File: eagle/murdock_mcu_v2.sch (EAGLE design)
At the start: 30 parts, among them IC1 MPU-9150, IC2 LT1763CS8-3.3, IC3 STM32F4XX_64, U1 USD-SOCKETNEW, X1 USBSMD, X2 MURDOCK_STACK

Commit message: updated labels
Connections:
- removed net A10: IC3G$2.PORTA_10, X2.SP1
- new net C11: IC3G$4.PORTC_11, X2.SP1
- net MISO: now also IC3G$3.PORTB_4; no longer IC3G$4.PORTC_11
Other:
- note added: "1_RX"
- note added: "UART4 = GPS"
- note added: "USART1 = SBUS"
- note added: "USART3 = SP1"
- note added: "USART6 = SP2"
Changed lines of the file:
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@@
 <plain>
 <text x="-93.98" y="60.96" size="1.778" layer="91">defined value on the bootloader pins</text>
+<text x="96.52" y="149.86" size="2.54" layer="94">UART4 = GPS</text>
+<text x="96.52" y="165.1" size="2.54" layer="94">USART1 = SBUS</text>
+<text x="96.52" y="139.7" size="2.54" layer="94">USART6 = SP2</text>
+<text x="96.52" y="157.48" size="2.54" layer="94">USART3 = SP1</text>
+<text x="17.78" y="127" size="1.778" layer="91">1_RX</text>
 </plain>
 <instances>
@@
 </segment>
 </net>
-<net name="A10" class="0">
-<segment>
-<pinref part="X2" gate="G$1" pin="SP1"/>
-<wire x1="96.52" y1="22.86" x2="86.36" y2="22.86" width="0.1524" layer="91"/>
-<label x="86.36" y="22.86" size="1.778" layer="95"/>
-</segment>
-<segment>
-<pinref part="IC3" gate="G$2" pin="PORTA_10"/>
-<wire x1="-17.78" y1="142.24" x2="-25.4" y2="142.24" width="0.1524" layer="91"/>
-<label x="-25.4" y="142.24" size="1.778" layer="95"/>
-</segment>
-</net>
 <net name="C7" class="0">
 <segment>
@@
 <net name="MISO" class="0">
 <segment>
-<pinref part="IC3" gate="G$4" pin="PORTC_11"/>
-<wire x1="-7.62" y1="48.26" x2="-17.78" y2="48.26" width="0.1524" layer="91"/>
-<label x="-17.78" y="48.26" size="1.778" layer="95"/>
-</segment>
-<segment>
 <pinref part="U1" gate="G$1" pin="DO"/>
 <wire x1="50.8" y1="27.94" x2="38.1" y2="27.94" width="0.1524" layer="91"/>
 <label x="38.1" y="27.94" size="1.778" layer="95"/>
+</segment>
+<segment>
+<pinref part="IC3" gate="G$3" pin="PORTB_4"/>
+<wire x1="38.1" y1="111.76" x2="30.48" y2="111.76" width="0.1524" layer="91"/>
+<label x="30.48" y="111.76" size="1.778" layer="95"/>
 </segment>
 </net>
@@
 </segment>
 </net>
+<net name="C11" class="0">
+<segment>
+<pinref part="IC3" gate="G$4" pin="PORTC_11"/>
+<wire x1="-7.62" y1="48.26" x2="-17.78" y2="48.26" width="0.1524" layer="91"/>
+<label x="-17.78" y="48.26" size="1.778" layer="95"/>
+</segment>
+<segment>
+<pinref part="X2" gate="G$1" pin="SP1"/>
+<wire x1="96.52" y1="22.86" x2="86.36" y2="22.86" width="0.1524" layer="91"/>
+<label x="86.36" y="22.86" size="1.778" layer="95"/>
+</segment>
+</net>
 </nets>
 </sheet>
-<sheet>
-<plain>
-</plain>
-<instances>
-</instances>
-<busses>
-</busses>
-<nets>
-</nets>
-</sheet>

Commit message: smaller updates
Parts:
- added IC4: BMP085, SparkFun-Sensors:BMP085
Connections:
- net +3V3: now also IC4.VDDA, IC4.VDDD
- net GND: now also IC4.GND
- net SCL: now also IC4.SCL
- net SDA: now also IC4.SDA
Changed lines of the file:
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@@
 <?xml version="1.0" encoding="utf-8"?>
 <!DOCTYPE eagle SYSTEM "eagle.dtd">
-<eagle version="6.2">
+<eagle version="6.4">
 <drawing>
 <settings>
@@
 <part name="GND27" library="supply1" deviceset="GND" device=""/>
 <part name="+3V6" library="supply1" deviceset="+3V3" device=""/>
+<part name="IC4" library="SparkFun-Sensors" deviceset="BMP085" device=""/>
+<part name="+3V11" library="supply1" deviceset="+3V3" device=""/>
+<part name="+3V12" library="supply1" deviceset="+3V3" device=""/>
+<part name="GND8" library="supply1" deviceset="GND" device=""/>
 </parts>
 <sheets>
@@
 <instance part="GND27" gate="1" x="170.18" y="152.4" rot="R270"/>
 <instance part="+3V6" gate="G$1" x="198.12" y="180.34"/>
+<instance part="IC4" gate="G$1" x="322.58" y="162.56" rot="R180"/>
+<instance part="+3V11" gate="G$1" x="335.28" y="162.56" rot="R270"/>
+<instance part="+3V12" gate="G$1" x="335.28" y="160.02" rot="R270"/>
+<instance part="GND8" gate="1" x="335.28" y="167.64" rot="R90"/>
 </instances>
 <busses>
@@
 <pinref part="GND27" gate="1" pin="GND"/>
 </segment>
+<segment>
+<pinref part="IC4" gate="G$1" pin="GND"/>
+<pinref part="GND8" gate="1" pin="GND"/>
+</segment>
 </net>
 <net name="+3V3" class="0">
@@
 <wire x1="200.66" y1="177.8" x2="198.12" y2="177.8" width="0.1524" layer="91"/>
 </segment>
+<segment>
+<pinref part="IC4" gate="G$1" pin="VDDD"/>
+<pinref part="+3V11" gate="G$1" pin="+3V3"/>
+</segment>
+<segment>
+<pinref part="IC4" gate="G$1" pin="VDDA"/>
+<pinref part="+3V12" gate="G$1" pin="+3V3"/>
+</segment>
 </net>
 <net name="+5V" class="0">
@@
 <pinref part="IC1" gate="G$1" pin="24"/>
 <label x="292.1" y="160.02" size="1.778" layer="95"/>
+<pinref part="IC4" gate="G$1" pin="SDA"/>
+<wire x1="309.88" y1="160.02" x2="292.1" y2="160.02" width="0.1524" layer="91"/>
 </segment>
 </net>
@@
 <pinref part="IC1" gate="G$1" pin="23"/>
 <label x="292.1" y="165.1" size="1.778" layer="95"/>
-</segment>
-</net>
+<wire x1="304.8" y1="165.1" x2="304.8" y2="162.56" width="0.1524" layer="91"/>
+<pinref part="IC4" gate="G$1" pin="SCL"/>
+<wire x1="304.8" y1="162.56" x2="309.88" y2="162.56" width="0.1524" layer="91"/>
+</segment>
+</net>

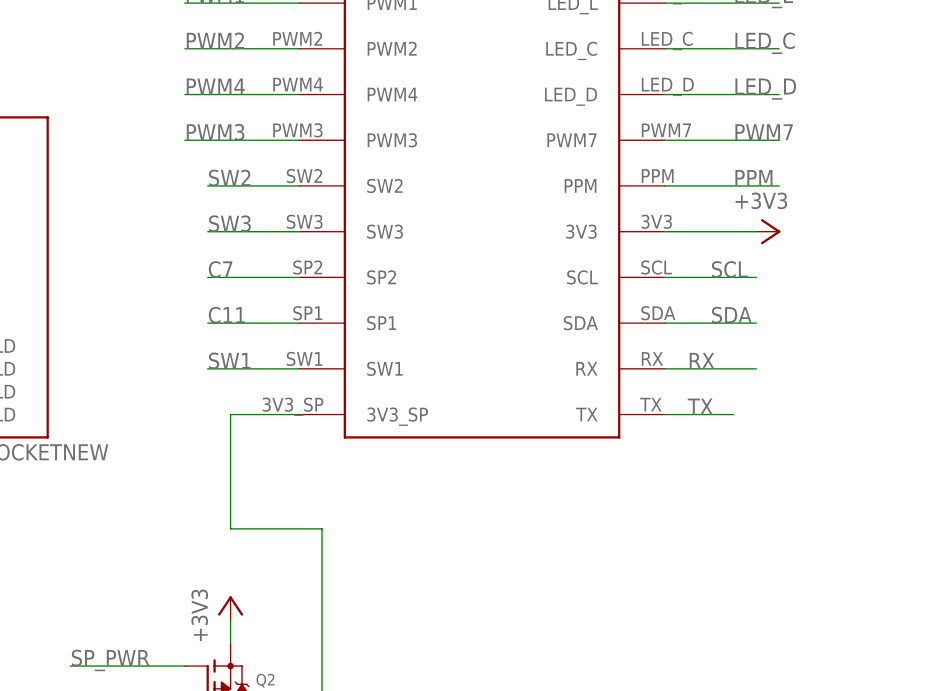
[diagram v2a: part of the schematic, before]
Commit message: updated stack schematic
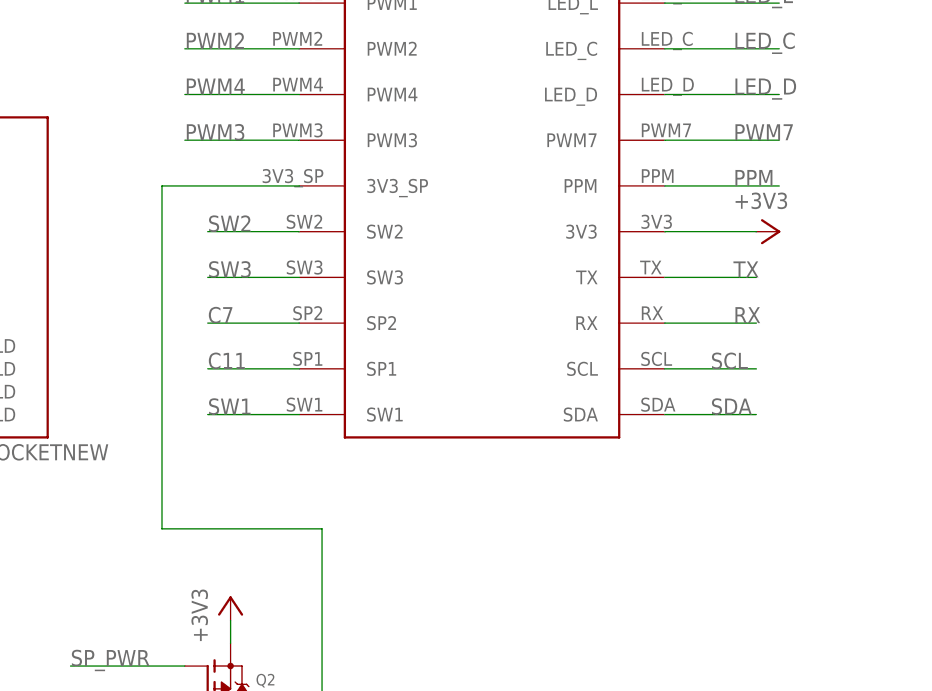
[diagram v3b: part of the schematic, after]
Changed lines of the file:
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@@
 <segment>
 <pinref part="X2" gate="G$1" pin="TX"/>
-<wire x1="137.16" y1="12.7" x2="144.78" y2="12.7" width="0.1524" layer="91"/>
-<label x="139.7" y="12.7" size="1.778" layer="95"/>
+<wire x1="137.16" y1="27.94" x2="147.32" y2="27.94" width="0.1524" layer="91"/>
+<label x="144.78" y="27.94" size="1.778" layer="95"/>
 </segment>
 <segment>
@@
 <segment>
 <pinref part="X2" gate="G$1" pin="RX"/>
-<wire x1="137.16" y1="17.78" x2="147.32" y2="17.78" width="0.1524" layer="91"/>
-<label x="139.7" y="17.78" size="1.778" layer="95"/>
+<wire x1="137.16" y1="22.86" x2="147.32" y2="22.86" width="0.1524" layer="91"/>
+<label x="144.78" y="22.86" size="1.778" layer="95"/>
 </segment>
 <segment>
@@
 <segment>
 <pinref part="X2" gate="G$1" pin="SP2"/>
-<wire x1="96.52" y1="27.94" x2="86.36" y2="27.94" width="0.1524" layer="91"/>
-<label x="86.36" y="27.94" size="1.778" layer="95"/>
+<wire x1="96.52" y1="22.86" x2="86.36" y2="22.86" width="0.1524" layer="91"/>
+<label x="86.36" y="22.86" size="1.778" layer="95"/>
 </segment>
 </net>
@@
 <segment>
 <pinref part="X2" gate="G$1" pin="SW1"/>
-<wire x1="96.52" y1="17.78" x2="86.36" y2="17.78" width="0.1524" layer="91"/>
-<label x="86.36" y="17.78" size="1.778" layer="95"/>
+<wire x1="96.52" y1="12.7" x2="86.36" y2="12.7" width="0.1524" layer="91"/>
+<label x="86.36" y="12.7" size="1.778" layer="95"/>
 </segment>
 <segment>
@@
 <segment>
 <pinref part="X2" gate="G$1" pin="SDA"/>
-<wire x1="137.16" y1="22.86" x2="147.32" y2="22.86" width="0.1524" layer="91"/>
-<label x="142.24" y="22.86" size="1.778" layer="95"/>
+<wire x1="137.16" y1="12.7" x2="147.32" y2="12.7" width="0.1524" layer="91"/>
+<label x="142.24" y="12.7" size="1.778" layer="95"/>
 </segment>
 <segment>
@@
 <segment>
 <pinref part="X2" gate="G$1" pin="SCL"/>
-<wire x1="137.16" y1="27.94" x2="147.32" y2="27.94" width="0.1524" layer="91"/>
-<label x="142.24" y="27.94" size="1.778" layer="95"/>
+<wire x1="137.16" y1="17.78" x2="147.32" y2="17.78" width="0.1524" layer="91"/>
+<label x="142.24" y="17.78" size="1.778" layer="95"/>
 </segment>
 <segment>
@@
 <segment>
 <pinref part="X2" gate="G$1" pin="SW3"/>
-<wire x1="96.52" y1="33.02" x2="86.36" y2="33.02" width="0.1524" layer="91"/>
-<label x="86.36" y="33.02" size="1.778" layer="95"/>
+<wire x1="96.52" y1="27.94" x2="86.36" y2="27.94" width="0.1524" layer="91"/>
+<label x="86.36" y="27.94" size="1.778" layer="95"/>
 </segment>
 <segment>
@@
 <segment>
 <pinref part="X2" gate="G$1" pin="SW2"/>
-<wire x1="96.52" y1="38.1" x2="86.36" y2="38.1" width="0.1524" layer="91"/>
-<label x="86.36" y="38.1" size="1.778" layer="95"/>
+<wire x1="96.52" y1="33.02" x2="86.36" y2="33.02" width="0.1524" layer="91"/>
+<label x="86.36" y="33.02" size="1.778" layer="95"/>
 </segment>
 <segment>
@@
 <wire x1="88.9" y1="-22.86" x2="99.06" y2="-22.86" width="0.1524" layer="91"/>
 <wire x1="99.06" y1="-22.86" x2="99.06" y2="0" width="0.1524" layer="91"/>
-<wire x1="99.06" y1="0" x2="88.9" y2="0" width="0.1524" layer="91"/>
-<wire x1="88.9" y1="0" x2="88.9" y2="12.7" width="0.1524" layer="91"/>
+<wire x1="99.06" y1="0" x2="81.28" y2="0" width="0.1524" layer="91"/>
+<wire x1="81.28" y1="0" x2="81.28" y2="38.1" width="0.1524" layer="91"/>
 <pinref part="X2" gate="G$1" pin="3V3_SP"/>
-<wire x1="88.9" y1="12.7" x2="96.52" y2="12.7" width="0.1524" layer="91"/>
+<wire x1="81.28" y1="38.1" x2="96.52" y2="38.1" width="0.1524" layer="91"/>
 </segment>
 </net>
@@
 <segment>
 <pinref part="X2" gate="G$1" pin="SP1"/>
-<wire x1="96.52" y1="22.86" x2="86.36" y2="22.86" width="0.1524" layer="91"/>
-<label x="86.36" y="22.86" size="1.778" layer="95"/>
-</segment>
-</net>
+<wire x1="96.52" y1="17.78" x2="86.36" y2="17.78" width="0.1524" layer="91"/>
+<label x="86.36" y="17.78" size="1.778" layer="95"/>
+</segment>
+</net>

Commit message: values
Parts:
- C1: value (none) -> 47µF/10V
- C10, C11: value (none) -> 2.2µF
- C12, C13: value (none) -> 15pF
- C2: value (none) -> 100µF/6V
- C3, C4, C5, C7: value (none) -> 100nF
- L1: value (none) -> 12Mhz
- Q2: value (none) -> PFET
- R1, R2: value (none) -> 33R
- R3: value (none) -> 0R
- R4, R5: value (none) -> 4k7
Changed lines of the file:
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@@
 <part name="P+1" library="supply1" deviceset="+5V" device=""/>
 <part name="+3V1" library="supply1" deviceset="+3V3" device=""/>
-<part name="C1" library="rcl" deviceset="CPOL-EU" device="SMCD"/>
-<part name="C2" library="rcl" deviceset="CPOL-EU" device="SMCD"/>
+<part name="C1" library="rcl" deviceset="CPOL-EU" device="SMCD" value="47µF/10V"/>
+<part name="C2" library="rcl" deviceset="CPOL-EU" device="SMCD" value="100µF/6V"/>
 <part name="+3V2" library="supply1" deviceset="+3V3" device=""/>
 <part name="+3V3" library="supply1" deviceset="+3V3" device=""/>
-<part name="C3" library="SparkFun-Capacitors" deviceset="CAP" device="0402-CAP"/>
-<part name="C4" library="SparkFun-Capacitors" deviceset="CAP" device="0402-CAP"/>
-<part name="C5" library="SparkFun-Capacitors" deviceset="CAP" device="0402-CAP"/>
-<part name="C7" library="SparkFun-Capacitors" deviceset="CAP" device="0402-CAP"/>
+<part name="C3" library="SparkFun-Capacitors" deviceset="CAP" device="0402-CAP" value="100nF"/>
+<part name="C4" library="SparkFun-Capacitors" deviceset="CAP" device="0402-CAP" value="100nF"/>
+<part name="C5" library="SparkFun-Capacitors" deviceset="CAP" device="0402-CAP" value="100nF"/>
+<part name="C7" library="SparkFun-Capacitors" deviceset="CAP" device="0402-CAP" value="100nF"/>
 <part name="+3V4" library="supply1" deviceset="+3V3" device=""/>
 <part name="GND11" library="SparkFun" deviceset="GND" device=""/>
-<part name="C10" library="SparkFun-Capacitors" deviceset="CAP" device="0805"/>
-<part name="C11" library="SparkFun-Capacitors" deviceset="CAP" device="0805"/>
+<part name="C10" library="SparkFun-Capacitors" deviceset="CAP" device="0805" value="2.2µF"/>
+<part name="C11" library="SparkFun-Capacitors" deviceset="CAP" device="0805" value="2.2µF"/>
 <part name="GND12" library="SparkFun-Aesthetics" deviceset="GND" device=""/>
 <part name="GND13" library="SparkFun-Aesthetics" deviceset="GND" device=""/>
 <part name="+3V5" library="supply1" deviceset="+3V3" device=""/>
-<part name="R1" library="SparkFun-Resistors" deviceset="RESISTOR" device="0402-RES"/>
-<part name="R2" library="SparkFun-Resistors" deviceset="RESISTOR" device="0402-RES"/>
-<part name="R3" library="SparkFun-Resistors" deviceset="RESISTOR" device="0402-RES"/>
-<part name="C12" library="SparkFun-Capacitors" deviceset="CAP" device="0402-CAP"/>
-<part name="C13" library="SparkFun-Capacitors" deviceset="CAP" device="0402-CAP"/>
-<part name="L1" library="seb" deviceset="X22-OSCILLATOR" device=""/>
+<part name="R1" library="SparkFun-Resistors" deviceset="RESISTOR" device="0402-RES" value="33R"/>
+<part name="R2" library="SparkFun-Resistors" deviceset="RESISTOR" device="0402-RES" value="33R"/>
+<part name="R3" library="SparkFun-Resistors" deviceset="RESISTOR" device="0402-RES" value="0R"/>
+<part name="C12" library="SparkFun-Capacitors" deviceset="CAP" device="0402-CAP" value="15pF"/>
+<part name="C13" library="SparkFun-Capacitors" deviceset="CAP" device="0402-CAP" value="15pF"/>
+<part name="L1" library="seb" deviceset="X22-OSCILLATOR" device="" value="12Mhz"/>
 <part name="GND14" library="SparkFun-Aesthetics" deviceset="GND" device=""/>
 <part name="GND15" library="SparkFun-Aesthetics" deviceset="GND" device=""/>
 <part name="P+2" library="supply1" deviceset="+5V" device=""/>
-<part name="Q2" library="microbuilder" deviceset="MOSFET-P" device=""/>
+<part name="Q2" library="microbuilder" deviceset="MOSFET-P" device="" value="PFET"/>
 <part name="+3V7" library="supply1" deviceset="+3V3" device=""/>
 <part name="GND17" library="supply1" deviceset="GND" device=""/>
@@
 <part name="GND22" library="supply1" deviceset="GND" device=""/>
 <part name="GND23" library="supply1" deviceset="GND" device=""/>
-<part name="R4" library="SparkFun" deviceset="RESISTOR" device="0402-RES"/>
-<part name="R5" library="SparkFun" deviceset="RESISTOR" device="0402-RES"/>
+<part name="R4" library="SparkFun" deviceset="RESISTOR" device="0402-RES" value="4k7"/>
+<part name="R5" library="SparkFun" deviceset="RESISTOR" device="0402-RES" value="4k7"/>
 <part name="+3V8" library="supply1" deviceset="+3V3" device=""/>
 <part name="+3V10" library="supply1" deviceset="+3V3" device=""/>

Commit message: note
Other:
- note added: "in case of 5V, pull up is neccessary (and proper pin configuraiotn)"
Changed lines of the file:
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@@
 <text x="96.52" y="157.48" size="2.54" layer="94">USART3 = SP1</text>
 <text x="17.78" y="127" size="1.778" layer="91">1_RX</text>
+<text x="93.98" y="-10.16" size="1.778" layer="91">in case of 5V, pull up is neccessary (and proper pin configuraiotn)</text>
 </plain>
 <instances>
